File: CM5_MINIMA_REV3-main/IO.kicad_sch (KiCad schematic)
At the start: 19 parts, among them J502 I2C, J503 SPI, J601 JST_SHBM04B-SRSS-TB, SW501 TS-1010A-B, SW601 B3U-3100-P, U1 LIS3DH, U602 SN74LVC1G14DBVR

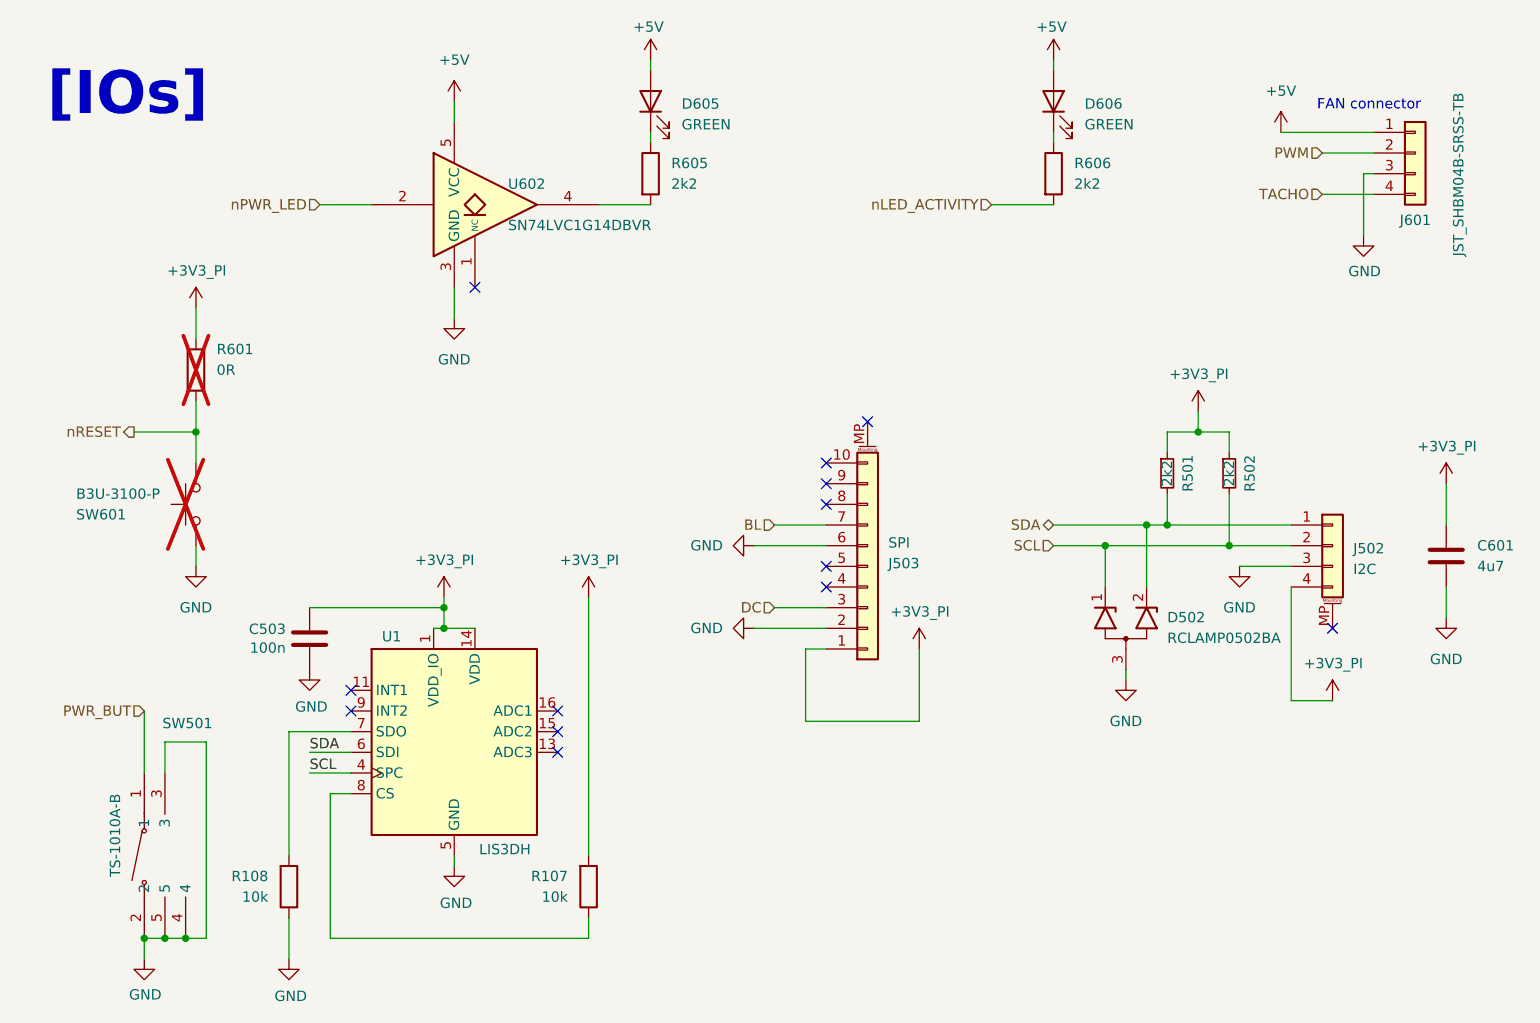
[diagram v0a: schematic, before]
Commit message: Revert CM5_MINIMA_REV3-main to pre-warning-fix state (feae2c2) - fix component mismatches
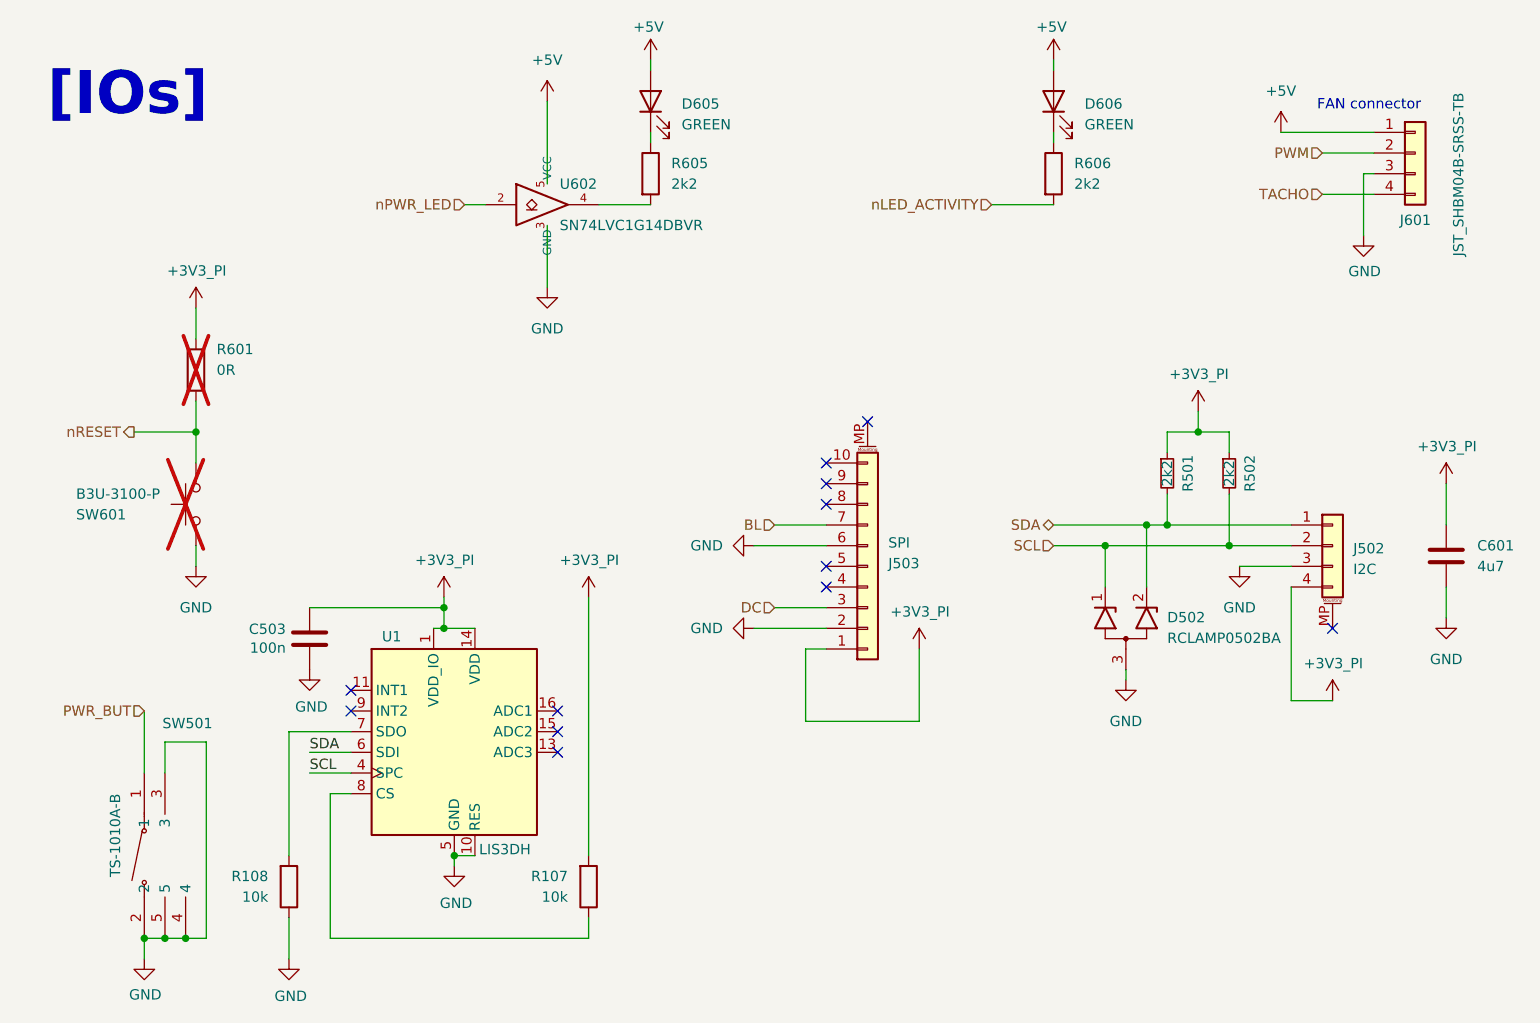
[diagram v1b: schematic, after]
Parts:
- D605, D606: footprint CM5_MINIMA_local:LED-SMD_L1.7-W0.6-RD -> EasyEDA:LED-SMD_L1.7-W0.6-RD
- SW501: footprint CM5_MINIMA_local:SW-SMD_TS-1010A-B -> EasyEDA:SW-SMD_TS-1010A-B
- U602: symbol 74xGxx:74LVC1G07 -> CM4IO:74LVC1G07_copy
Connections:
- no-connect marks 13 -> 12
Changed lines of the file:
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@@
 	)
 	(junction
+		(at 64.77 115.57)
+		(diameter 0)
+		(color 0 0 0 0)
+	)
+	(junction
 		(at 33.02 63.5)
 		(diameter 0)
@@
 	)
 	(no_connect
-		(at 67.31 45.72)
-	)
-	(no_connect
 		(at 115.57 62.23)
 	)
@@
 	(wire
 		(pts
-			(xy 48.26 35.56) (xy 54.61 35.56)
+			(xy 66.04 35.56) (xy 68.58 35.56)
 		)
 		(stroke
@@
 	(wire
 		(pts
+			(xy 76.2 33.02) (xy 76.2 22.86)
+		)
+		(stroke
+			(width 0)
+			(type solid)
+		)
+	)
+	(wire
+		(pts
 			(xy 33.02 59.69) (xy 33.02 63.5)
 		)
@@
 	(wire
 		(pts
+			(xy 64.77 115.57) (xy 67.31 115.57)
+		)
+		(stroke
+			(width 0)
+			(type default)
+		)
+	)
+	(wire
+		(pts
 			(xy 160.02 71.12) (xy 160.02 77.47)
 		)
@@
 	(wire
 		(pts
+			(xy 88.9 35.56) (xy 82.55 35.56)
+		)
+		(stroke
+			(width 0)
+			(type solid)
+		)
+	)
+	(wire
+		(pts
 			(xy 63.5 83.82) (xy 63.5 85.09)
 		)
@@
 	(wire
 		(pts
-			(xy 64.77 22.86) (xy 64.77 25.4)
-		)
-		(stroke
-			(width 0)
-			(type default)
-		)
-	)
-	(wire
-		(pts
 			(xy 34.29 101.6) (xy 34.29 125.73)
 		)
@@
 	(wire
 		(pts
-			(xy 82.55 35.56) (xy 88.9 35.56)
-		)
-		(stroke
-			(width 0)
-			(type default)
-		)
-	)
-	(wire
-		(pts
 			(xy 144.78 77.47) (xy 138.43 77.47)
 		)
@@
 	(wire
 		(pts
-			(xy 186.69 82.55) (xy 186.69 86.36)
+			(xy 76.2 38.1) (xy 76.2 45.72)
 		)
 		(stroke
@@
 	(wire
 		(pts
-			(xy 177.8 31.75) (xy 176.53 31.75)
+			(xy 186.69 82.55) (xy 186.69 86.36)
 		)
 		(stroke
@@
 	(wire
 		(pts
-			(xy 161.29 80.01) (xy 167.64 80.01)
+			(xy 177.8 31.75) (xy 176.53 31.75)
 		)
 		(stroke
@@
 	(wire
 		(pts
-			(xy 144.78 77.47) (xy 144.78 82.55)
+			(xy 161.29 80.01) (xy 167.64 80.01)
 		)
 		(stroke
@@
 	(wire
 		(pts
-			(xy 64.77 45.72) (xy 64.77 49.53)
+			(xy 144.78 77.47) (xy 144.78 82.55)
 		)
 		(stroke
@@
 	(hierarchical_label "nPWR_LED"
 		(shape input)
-		(at 48.26 35.56 180)
+		(at 66.04 35.56 180)
 		(effects
 			(font
@@
 			)
 		)
-		(property "Footprint" "CM5_MINIMA_local:SW-SMD_TS-1010A-B"
+		(property "Footprint" "EasyEDA:SW-SMD_TS-1010A-B"
 			(at 39.37 115.57 0)
 			(effects
@@
 	(symbol
 		(lib_id "power:+5V")
-		(at 64.77 22.86 0)
+		(at 76.2 22.86 0)
 		(unit 1)
 		(exclude_from_sim no)
@@
 		(fields_autoplaced yes)
 		(property "Reference" "#PWR0516"
-			(at 64.77 26.67 0)
+			(at 76.2 26.67 0)
 			(effects
 				(font
@@
 		)
 		(property "Value" "+5V"
-			(at 64.77 17.78 0)
+			(at 76.2 17.78 0)
 			(effects
 				(font
@@
 		)
 		(property "Footprint" ""
-			(at 64.77 22.86 0)
+			(at 76.2 22.86 0)
 			(effects
 				(font
@@
 		)
 		(property "Datasheet" ""
-			(at 64.77 22.86 0)
+			(at 76.2 22.86 0)
 			(effects
 				(font
@@
 		)
 		(property "Description" "Power symbol creates a global label with name \"+5V\""
-			(at 64.77 22.86 0)
+			(at 76.2 22.86 0)
 			(effects
 				(font
@@
 	)
 	(symbol
-		(lib_name "R_Small_1")
 		(lib_id "Device:R_Small")
 		(at 152.4 68.58 0)
@@
 			)
 		)
-		(property "Datasheet" "~"
+		(property "Datasheet" ""
 			(at 152.4 68.58 0)
 			(effects
@@
 			)
 		)
-		(property "Description" "Resistor, small symbol"
+		(property "Description" ""
 			(at 152.4 68.58 0)
 			(effects
@@
 			)
 		)
-		(property "Datasheet" "~"
+		(property "Datasheet" ""
 			(at 160.02 68.58 0)
 			(effects
@@
 			)
 		)
-		(property "Description" "Resistor, small symbol"
+		(property "Description" ""
 			(at 160.02 68.58 0)
 			(effects
@@
 		(fields_autoplaced yes)
 		(property "Reference" "D606"
-			(at 142.24 23.1774 90)
+			(at 142.24 23.1775 90)
 			(effects
 				(font
@@
 		)
 		(property "Value" "GREEN"
-			(at 142.24 25.7174 90)
+			(at 142.24 25.7175 90)
 			(effects
 				(font
@@
 			)
 		)
-		(property "Footprint" "CM5_MINIMA_local:LED-SMD_L1.7-W0.6-RD"
+		(property "Footprint" "EasyEDA:LED-SMD_L1.7-W0.6-RD"
 			(at 138.43 22.86 0)
 			(effects
@@
 			)
 		)
-		(property "Datasheet" "~"
+		(property "Datasheet" ""
 			(at 138.43 22.86 0)
 			(effects
@@
 			)
 		)
-		(property "Description" "Light emitting diode"
+		(property "Description" ""
 			(at 138.43 22.86 0)
 			(effects
@@
 			)
 		)
-		(property "Sim.Pins" "1=K 2=A"
-			(at 138.43 22.86 0)
-			(effects
-				(font
-					(size 1.27 1.27)
-				)
-				(hide yes)
-			)
-		)
 		(pin "1"
 		)
@@
 	(symbol
 		(lib_id "power:GND")
-		(at 64.77 49.53 0)
+		(at 76.2 45.72 0)
 		(unit 1)
 		(exclude_from_sim no)
@@
 		(fields_autoplaced yes)
 		(property "Reference" "#PWR0607"
-			(at 64.77 55.88 0)
+			(at 76.2 52.07 0)
 			(effects
 				(font
@@
 		)
 		(property "Value" "GND"
-			(at 64.77 54.61 0)
+			(at 76.2 50.8 0)
 			(effects
 				(font
@@
 		)
 		(property "Footprint" ""
-			(at 64.77 49.53 0)
+			(at 76.2 45.72 0)
 			(effects
 				(font
@@
 		)
 		(property "Datasheet" ""
-			(at 64.77 49.53 0)
+			(at 76.2 45.72 0)
 			(effects
 				(font
@@
 		)
 		(property "Description" "Power symbol creates a global label with name \"GND\" , ground"
-			(at 64.77 49.53 0)
+			(at 76.2 45.72 0)
 			(effects
 				(font
@@
 	)
 	(symbol
-		(lib_id "74xGxx:74LVC1G07")
-		(at 69.85 35.56 0)
+		(lib_name "74LVC1G07_copy_1")
+		(lib_id "CM4IO:74LVC1G07_copy")
+		(at 76.2 35.56 0)
 		(unit 1)
 		(exclude_from_sim no)
@@
 		(dnp no)
 		(property "Reference" "U602"
-			(at 71.374 33.02 0)
+			(at 77.724 33.02 0)
 			(effects
 				(font
@@
 		)
 		(property "Value" "SN74LVC1G14DBVR"
-			(at 71.374 38.1 0)
+			(at 77.724 38.1 0)
 			(effects
 				(font
@@
 		)
 		(property "Footprint" "Package_TO_SOT_SMD:SOT-353_SC-70-5"
-			(at 69.85 35.56 0)
+			(at 76.2 35.56 0)
 			(effects
 				(font
@@
 			)
 		)
-		(property "Datasheet" "https://www.ti.com/lit/ds/symlink/sn74lvc1g07.pdf"
-			(at 69.85 35.56 0)
+		(property "Datasheet" "https://www.lcsc.com/datasheet/lcsc_datasheet_2405141143_UMW-Youtai-Semiconductor-Co---Ltd--SN74LVC1G14DBVR_C434069.pdf"
+			(at 76.2 35.56 0)
 			(effects
 				(font
@@
 			)
 		)
-		(property "Description" "Single Buffer Gate, Open Drain, Low-Voltage CMOS"
-			(at 69.85 35.56 0)
+		(property "Description" ""
+			(at 76.2 35.56 0)
 			(effects
 				(font
@@
 		)
 		(property "Part Description" "Buffer, Non-Inverting 1 Element 1 Bit per Element Open Drain Output SOT-353"
-			(at 69.85 35.56 0)
+			(at 76.2 35.56 0)
 			(effects
 				(font
@@
 		)
 		(property "P/N" "SN74LVC1G14DBVR"
-			(at 69.85 35.56 0)
+			(at 76.2 35.56 0)
 			(effects
 				(font
@@
 	)
 	(symbol
-		(lib_name "LED_1")
 		(lib_id "Device:LED")
 		(at 88.9 22.86 90)
@@
 		(fields_autoplaced yes)
 		(property "Reference" "D605"
-			(at 92.71 23.1774 90)
+			(at 92.71 23.1775 90)
 			(effects
 				(font
@@
 		)
 		(property "Value" "GREEN"
-			(at 92.71 25.7174 90)
+			(at 92.71 25.7175 90)
 			(effects
 				(font
@@
 			)
 		)
-		(property "Footprint" "CM5_MINIMA_local:LED-SMD_L1.7-W0.6-RD"
+		(property "Footprint" "EasyEDA:LED-SMD_L1.7-W0.6-RD"
 			(at 88.9 22.86 0)
 			(effects
@@
 			)
 		)
-		(property "Datasheet" "~"
+		(property "Datasheet" ""
 			(at 88.9 22.86 0)
 			(effects
@@
 			)
 		)
-		(property "Description" "Light emitting diode"
+		(property "Description" ""
 			(at 88.9 22.86 0)
 			(effects
@@
 			(at 88.9 22.86 0)
 			(effects
-				(font
-					(size 1.27 1.27)
-				)
-				(hide yes)
-			)
-		)
-		(property "Sim.Pins" "1=K 2=A"
-			(at 88.9 22.86 0)
-			(effects

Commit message: with old version retraced and fixing
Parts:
- U602: symbol CM4IO:74LVC1G07_copy -> CM5IO:74LVC1G07_copy
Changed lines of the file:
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@@
 	)
 	(junction
-		(at 31.75 125.73)
-		(diameter 0)
-		(color 0 0 0 0)
-	)
-	(junction
 		(at 156.21 63.5)
 		(diameter 0)
@@
 	)
 	(junction
-		(at 26.67 125.73)
+		(at 64.77 115.57)
 		(diameter 0)
 		(color 0 0 0 0)
 	)
 	(junction
-		(at 64.77 115.57)
+		(at 33.02 63.5)
 		(diameter 0)
 		(color 0 0 0 0)
 	)
 	(junction
-		(at 33.02 63.5)
+		(at 31.75 125.73)
 		(diameter 0)
 		(color 0 0 0 0)
 	)
 	(junction
-		(at 29.21 125.73)
+		(at 63.5 85.09)
 		(diameter 0)
 		(color 0 0 0 0)
 	)
 	(junction
-		(at 63.5 85.09)
+		(at 29.21 125.73)
 		(diameter 0)
 		(color 0 0 0 0)
@@
 	(wire
 		(pts
-			(xy 31.75 125.73) (xy 34.29 125.73)
-		)
-		(stroke
-			(width 0)
-			(type default)
-		)
-	)
-	(wire
-		(pts
 			(xy 66.04 35.56) (xy 68.58 35.56)
 		)
@@
 	(wire
 		(pts
-			(xy 52.07 100.33) (xy 44.45 100.33)
+			(xy 29.21 125.73) (xy 31.75 125.73)
 		)
 		(stroke
@@
 	(wire
 		(pts
-			(xy 33.02 63.5) (xy 33.02 67.31)
+			(xy 52.07 100.33) (xy 44.45 100.33)
 		)
 		(stroke
@@
 	(wire
 		(pts
-			(xy 29.21 125.73) (xy 31.75 125.73)
+			(xy 33.02 63.5) (xy 33.02 67.31)
 		)
 		(stroke
@@
 	(wire
 		(pts
+			(xy 31.75 125.73) (xy 34.29 125.73)
+		)
+		(stroke
+			(width 0)
+			(type default)
+		)
+	)
+	(wire
+		(pts
 			(xy 121.92 99.06) (xy 121.92 90.17)
 		)
@@
 	)
 	(symbol
-		(lib_name "74LVC1G07_copy_1")
-		(lib_id "CM4IO:74LVC1G07_copy")
+		(lib_id "CM5IO:74LVC1G07_copy")
 		(at 76.2 35.56 0)
 		(unit 1)
@@
 			)
 		)
-		(property "Datasheet" "https://www.lcsc.com/datasheet/lcsc_datasheet_2405141143_UMW-Youtai-Semiconductor-Co---Ltd--SN74LVC1G14DBVR_C434069.pdf"
+		(property "Datasheet" "http://www.ti.com/lit/sg/scyt129e/scyt129e.pdf"
 			(at 76.2 35.56 0)
 			(effects
@@
 			)
 		)
-		(property "Description" ""
+		(property "Description" "Single Buffer Gate w/ Open Drain, Low-Voltage CMOS"
 			(at 76.2 35.56 0)
 			(effects
@@
 	)
 	(symbol
+		(lib_name "LED_1")
 		(lib_id "Device:LED")
 		(at 88.9 22.86 90)
@@
 		(fields_autoplaced yes)
 		(property "Reference" "D605"
-			(at 92.71 23.1775 90)
+			(at 92.71 23.1774 90)
 			(effects
 				(font
@@
 		)
 		(property "Value" "GREEN"
-			(at 92.71 25.7175 90)
+			(at 92.71 25.7174 90)
 			(effects
 				(font
@@
 			)
 		)
-		(property "Datasheet" ""
+		(property "Datasheet" "~"
 			(at 88.9 22.86 0)
 			(effects
@@
 			)
 		)
-		(property "Description" ""
+		(property "Description" "Light emitting diode"
 			(at 88.9 22.86 0)
 			(effects
@@
 			(at 88.9 22.86 0)
 			(effects
+				(font
+					(size 1.27 1.27)
+				)
+				(hide yes)
+			)
+		)
+		(property "Sim.Pins" "1=K 2=A"
+			(at 88.9 22.86 0)
+			(effects
